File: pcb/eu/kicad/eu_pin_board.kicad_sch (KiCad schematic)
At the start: 8 parts, among them J1 Socket 1x2 2.54, P1 P70-2200045 GND, P2 P70-2200045 +5V, P3 P70-2200045 +5V, P4 P70-2200045 GND

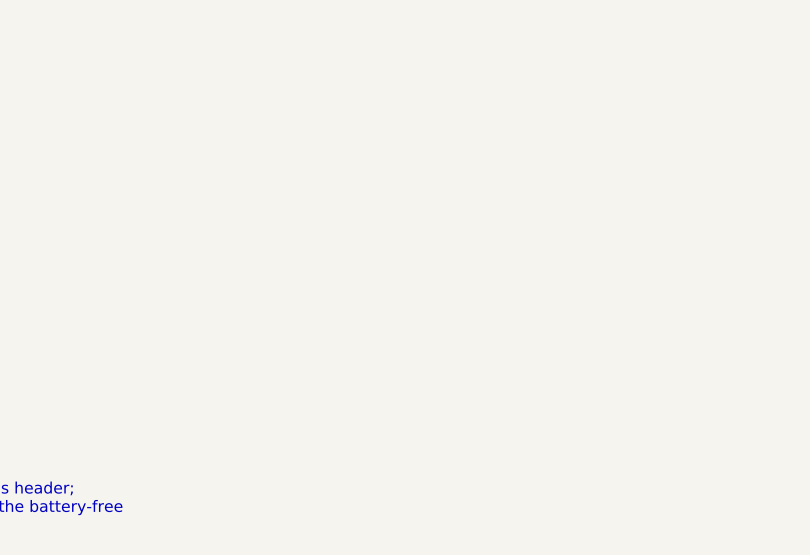
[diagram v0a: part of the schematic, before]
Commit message: v0.6: one barrier per variant, EU ridges, NA cable slit, ElegooSlicer projects, back cover and plate fixes (D-127..D-150)
- One barrier per variant for every edition; printed blank board in switch only (D-127..D-131)
- EU pin board ridge loop and blank board ridge; more pin board bosses (D-128..D-133)
- NA face plate lobes round the screws form the pocket's ends (D-132)
- NA 5 V cable straight from J2 to J1 through a slit in the barrier's bottom wall, 50 mm FFC; MH3 back in line;
  slit open in battery-free and switch only (D-134, D-135)
- Back cover: flex pad section 1.5 mm in, rim cut at the bottom end with a 0.08 mm-layer taper, steel plate clips
  solid in the shell, bottom clip lead-in 45 deg, pry notch 1.5 deep (D-136..D-143, D-145, D-147)
- 45 deg chamfer round the remote pocket's mouth (D-139)
- Print projects built with ElegooSlicer 1.5.3.5, overrides also as object settings (D-144)
- EU plain face plate 84.6 x 84.6, plain carrier whole on all sides with the full rim (D-146, D-150)
- Steel piece 1.0 mm thick, recess 1.2 deep (D-148)
- MSR-2 12 mm left, grille on the plate's centre line; ant logos in the sensor boards' lower-left corners (D-149)
- Repo URL github.com/antevens/sladdseg on the boards
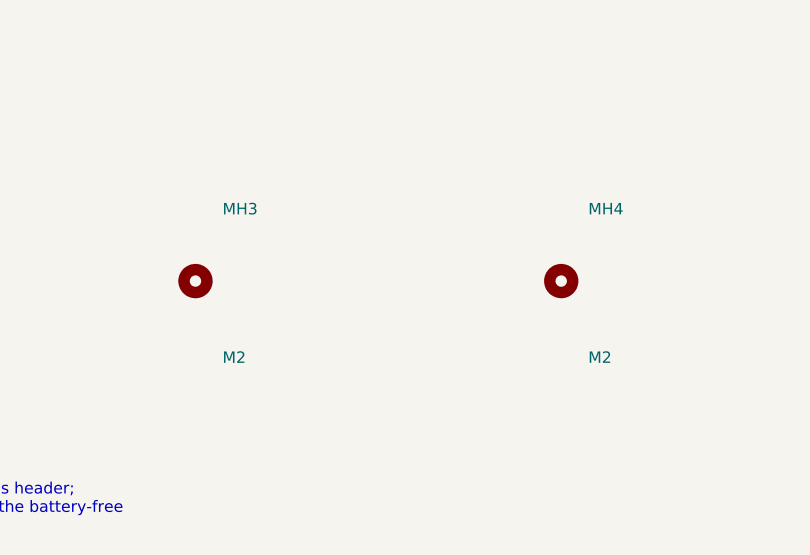
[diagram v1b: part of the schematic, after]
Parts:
- added MH3, MH4: M2, eu_mains:MountingHole_2.2mm_M2, symbol eu_mains:MountingHole
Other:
- company: smart-wallplate -> sladdseg
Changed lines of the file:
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@@
 		(date "2026-10-12")
 		(rev "v0.6")
-		(company "smart-wallplate")
+		(company "sladdseg")
 		(comment 1 "Generated by pcb/eu/tools/gen_eu.py - edit parts_eu.py")
 	)
@@
 					(unit 1)
 				)
+			)
+		)
+	)
+	(symbol
+		(lib_id "eu_mains:MountingHole")
+		(at 116.84 157.48 0)
+		(unit 1)
+		(exclude_from_sim no)
+		(in_bom no)
+		(on_board yes)
+		(dnp no)
+		(property "Reference" "MH3"
+			(at 119.84 149.48 0)
+			(effects
+				(font
+					(size 1.27 1.27)
+				)
+				(justify left)
+			)
+		)
+		(property "Value" "M2"
+			(at 119.84 165.98 0)
+			(effects
+				(font
+					(size 1.27 1.27)
+				)
+				(justify left)
+			)
+		)
+		(property "Footprint" "eu_mains:MountingHole_2.2mm_M2"
+			(at 116.84 157.48 0)
+			(effects
+				(font
+					(size 1.27 1.27)
+				)
+				(hide yes)
+			)
+		)
+		(property "Datasheet" ""
+			(at 116.84 157.48 0)
+			(effects
+				(font
+					(size 1.27 1.27)
+				)
+				(hide yes)
+			)
+		)
+		(property "Description" "M2 to the barrier boss"
+			(at 116.84 157.48 0)
+			(effects
+				(font
+					(size 1.27 1.27)
+				)
+				(hide yes)
+			)
+		)
+		(property "Manufacturer" "-"
+			(at 116.84 157.48 0)
+			(effects
+				(font
+					(size 1.27 1.27)
+				)
+				(hide yes)
+			)
+		)
+		(property "MPN" "-"
+			(at 116.84 157.48 0)
+			(effects
+				(font
+					(size 1.27 1.27)
+				)
+				(hide yes)
+			)
+		)
+		(instances
+			(project "eu_pin_board"
+				(path "/1c5833ef-209b-5298-b126-1a6c4647ab2c"
+					(reference "MH3")
+					(unit 1)
+				)
+			)
+		)
+	)
+	(symbol
+		(lib_id "eu_mains:MountingHole")
+		(at 157.48 157.48 0)
+		(unit 1)
+		(exclude_from_sim no)
+		(in_bom no)
+		(on_board yes)
+		(dnp no)
+		(property "Reference" "MH4"
+			(at 160.48 149.48 0)
+			(effects
+				(font
+					(size 1.27 1.27)
+				)
+				(justify left)
+			)
+		)
+		(property "Value" "M2"
+			(at 160.48 165.98 0)
+			(effects
+				(font
+					(size 1.27 1.27)
+				)
+				(justify left)
+			)
+		)
+		(property "Footprint" "eu_mains:MountingHole_2.2mm_M2"
+			(at 157.48 157.48 0)
+			(effects
+				(font
+					(size 1.27 1.27)
+				)
+				(hide yes)
+			)
+		)
+		(property "Datasheet" ""
+			(at 157.48 157.48 0)
+			(effects
+				(font
+					(size 1.27 1.27)
+				)
+				(hide yes)
+			)
+		)
+		(property "Description" "M2 to the barrier boss"
+			(at 157.48 157.48 0)
+			(effects
+				(font
+					(size 1.27 1.27)
+				)
+				(hide yes)
+			)
+		)
+		(property "Manufacturer" "-"
+			(at 157.48 157.48 0)
+			(effects
+				(font
+					(size 1.27 1.27)
+				)
+				(hide yes)
+			)
+		)
+		(property "MPN" "-"
+			(at 157.48 157.48 0)
+			(effects
+				(font
+					(size 1.27 1.27)
+				)
+				(hide yes)
+			)
+		)
+		(instances
+			(project "eu_pin_board"
+				(path "/1c5833ef-209b-5298-b126-1a6c4647ab2c"
+					(reference "MH4")
+					(unit 1)
+				)
